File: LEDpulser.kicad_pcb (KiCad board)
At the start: 2 copper layers, 50.8 x 77.7 mm, 84 parts, among them J1 RJHSE-5380, J2 EPS.00.250.NTN, J3 EPS.00.250.NTN, J4 EB21A-04-D, J5 EPL.0S.302.HLN, Q1 DMP32D4S, Q2 DMN3028LQ-7, Q3 DMN3028LQ-7, SW1 BST11T2AVR, U1 74AHCT123APW,118, U10 LT3082EST#TRPBF, U2 74AHCT123APW,118, U3 74AHCT123APW,118, U4 SN74LVC2G74, U5 LT1117, U6 IXDI602SIATR, U7 NE555S-13, U8 PM8834, U9 PM8834

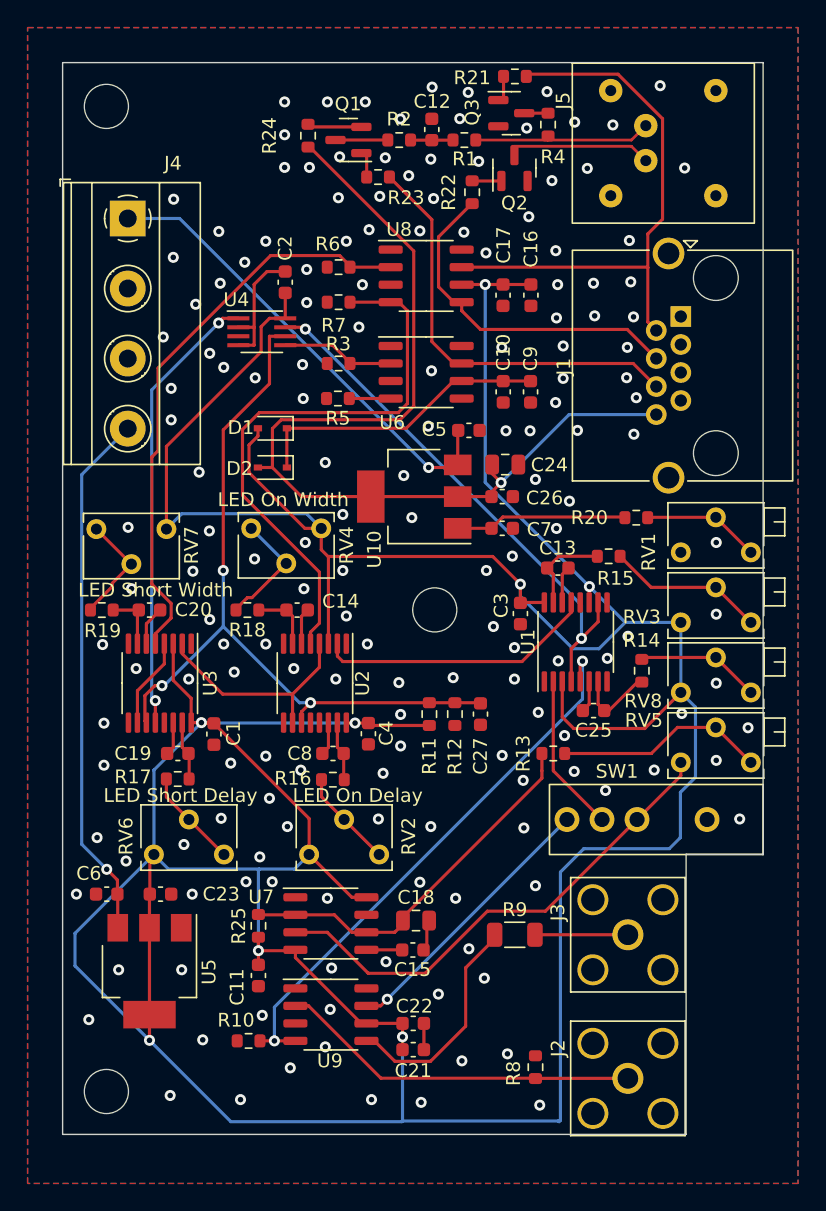
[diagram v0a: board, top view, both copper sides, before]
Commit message: Added guard ring around 0-20V regulator set pin and output to set current shunt.
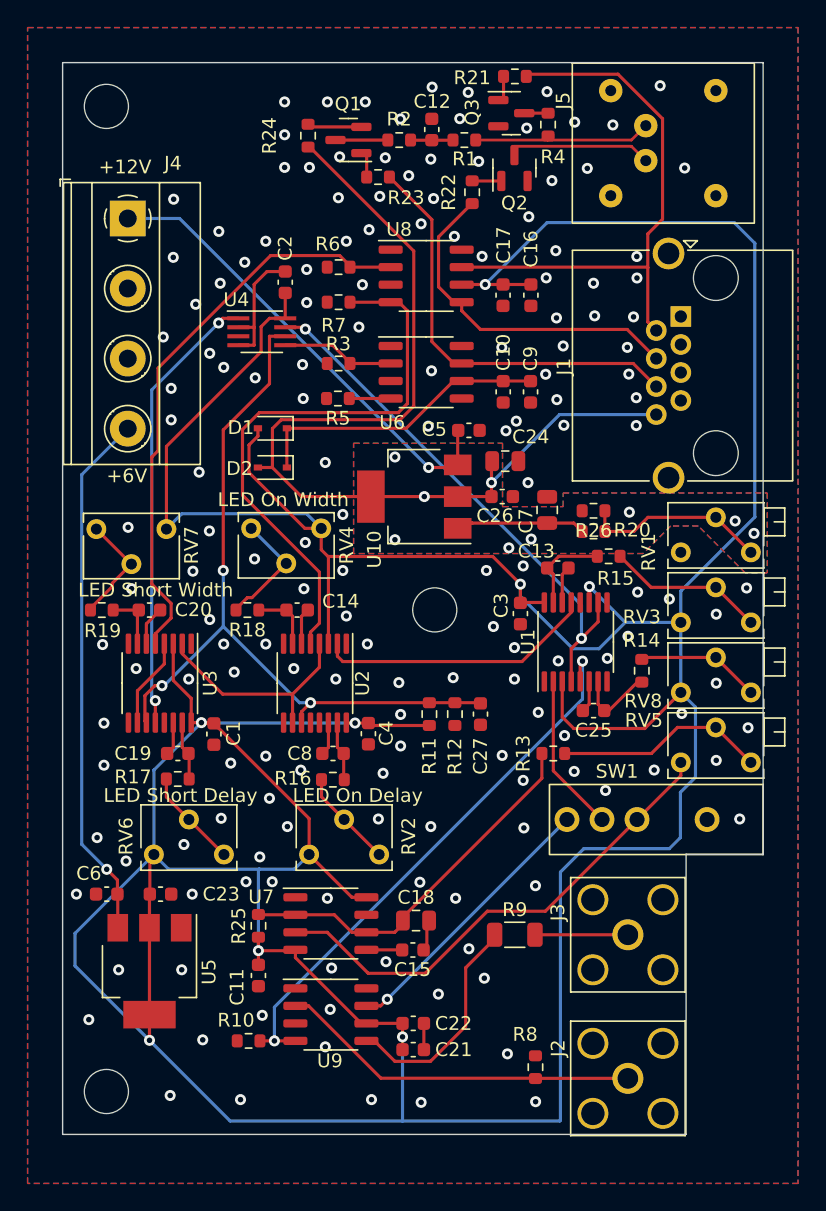
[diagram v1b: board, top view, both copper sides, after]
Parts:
- added R26: DNP, Resistor_SMD:R_0603_1608Metric, F.Cu at (127.4, 57.9)
- C7: value 1uF -> 0.1uF; footprint Capacitor_SMD:C_0603_1608Metric -> Capacitor_SMD:C_0805_2012Metric
- moved C7 3.52 mm to (124.0, 57.8), turned to 90 degrees
- moved R20 3.26 mm to (127.4, 59.4)
- moved C24 0.25 mm to (121.0, 54.3)
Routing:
- net VCC: track 335.3 -> 361.9 mm
- net Net-(R20-Pad1): track 8.55 -> 13.6 mm
- net Net-(C7-Pad1): track 12.5 -> 9.96 mm
- net /CAP_VOLTAGE_OUT: track 69.6 -> 70.1 mm, vias 1 -> 9
- net GND: vias 169 -> 165
- added copper zone on B.Cu, net /CAP_VOLTAGE_OUT
- added copper zone on F.Cu, net /CAP_VOLTAGE_OUT
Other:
- board text added: "+12V"

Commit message: Minor layout edits and generation of fabrication files.
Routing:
- net Net-(C7-Pad1): track 9.96 -> 9.43 mm
- net /CAP_VOLTAGE_OUT: track 70.1 -> 70.0 mm, vias 9 -> 10

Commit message: Added pdf schematic.
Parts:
- D1, D2: value CUS08F30,H3F -> CUS08F30
- U1, U2, U3: value 74AHCT123APW,118 -> 74AHCT123
- U10: value LT3082EST#TRPBF -> LT3082
- U6: value IXDI602SIATR -> IXDI602
- U7: value NE555S-13 -> NE555S

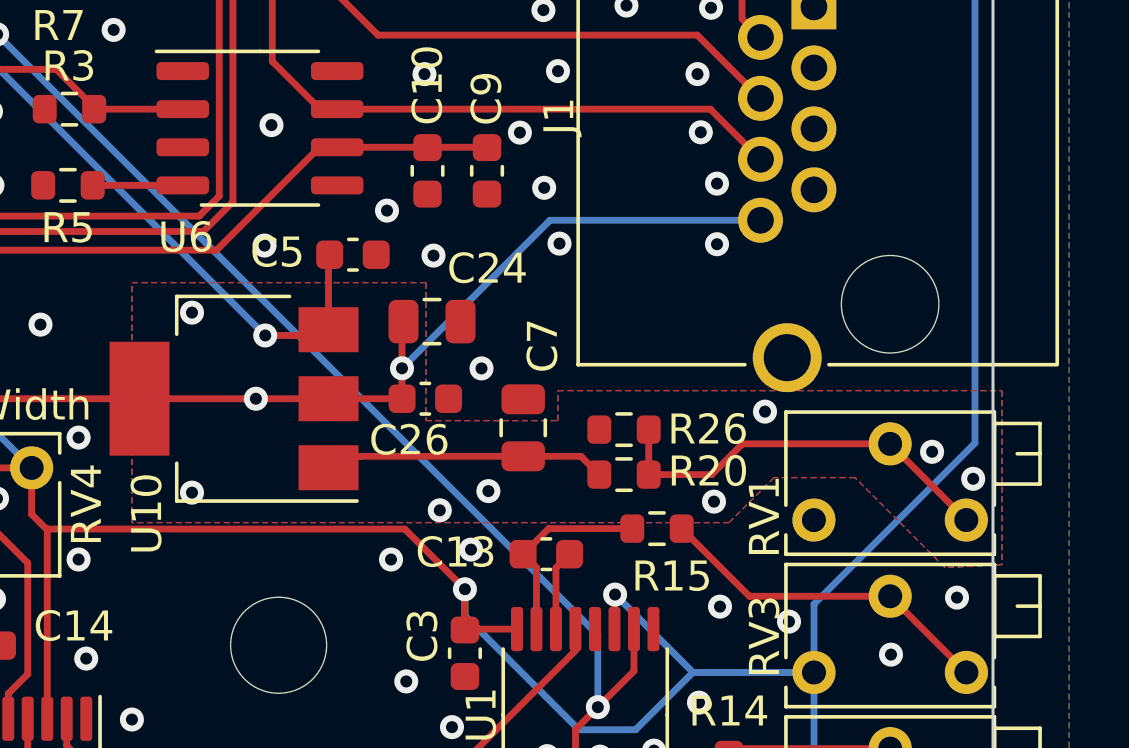
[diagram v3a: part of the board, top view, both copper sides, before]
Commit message: Fixed issue with shorts on RJ-45 connector shorting out HV regulator.
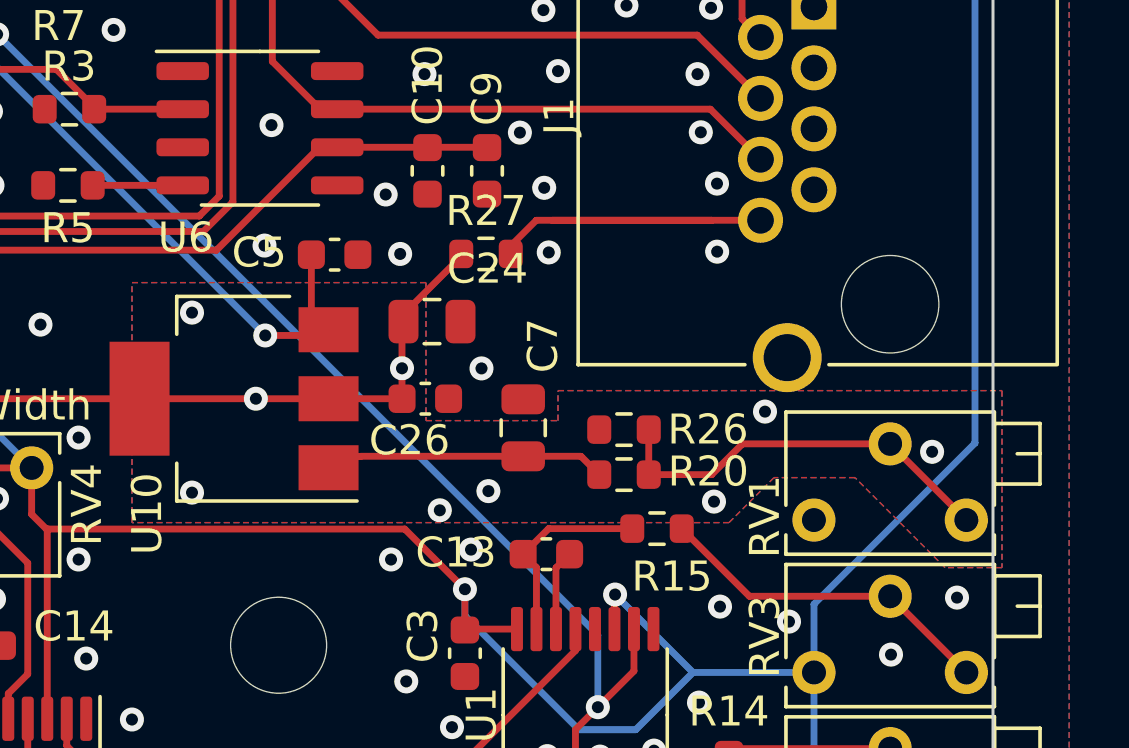
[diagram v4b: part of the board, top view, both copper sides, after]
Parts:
- added R27: 10k, Resistor_SMD:R_0603_1608Metric, F.Cu at (122.8, 52.0)
- D1, D2: value CUS08F30 -> CUS08F30,H3F
- R4: value 50 -> 0
- RV1: value 2Meg -> 100k
- U1, U2, U3: value 74AHCT123 -> 74AHCT123APW,118
- U10: value LT3082 -> LT3082EST#TRPBF
- U6: value IXDI602 -> IXDN602SIATR
- U7: value NE555S -> NE555S-13
- moved C5 0.61 mm to (117.8, 52.1)
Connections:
- C24 pad 1: /CAP_VOLTAGE_OUT -> /CAP_VOLTAGE
- C26 pad 1: /CAP_VOLTAGE_OUT -> /CAP_VOLTAGE
- D2 pad 2: /CAP_VOLTAGE_OUT -> /CAP_VOLTAGE
- R24 pad 2: /CAP_VOLTAGE_OUT -> /CAP_VOLTAGE
- R26 pad 2: /CAP_VOLTAGE_OUT -> /CAP_VOLTAGE
- U10 pad 2: /CAP_VOLTAGE_OUT -> /CAP_VOLTAGE
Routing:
- net /CAP_VOLTAGE: track 0.00 -> 60.1 mm, vias 0 -> 9
- net /CAP_VOLTAGE_OUT: track 70.0 -> 14.4 mm, vias 10 -> 0
- added copper zone on B.Cu, net /CAP_VOLTAGE
- added copper zone on F.Cu, net /CAP_VOLTAGE
- removed copper zone on B.Cu, net /CAP_VOLTAGE_OUT
- removed copper zone on F.Cu, net /CAP_VOLTAGE_OUT
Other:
- board text added: "LED Pulser v3"
- board text removed: "LED Pulser v2"

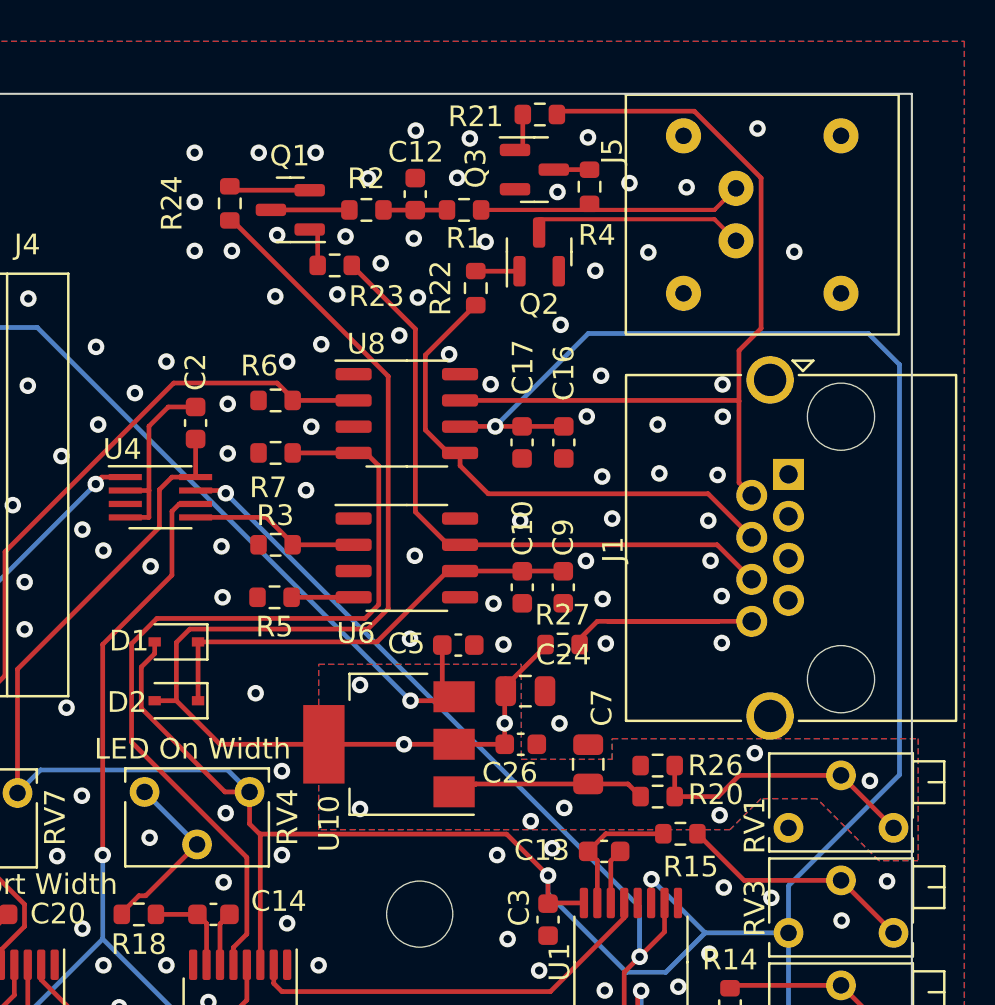
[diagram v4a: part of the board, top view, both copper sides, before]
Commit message: Added resistors to prevent shorting power through outputs on RJ45.
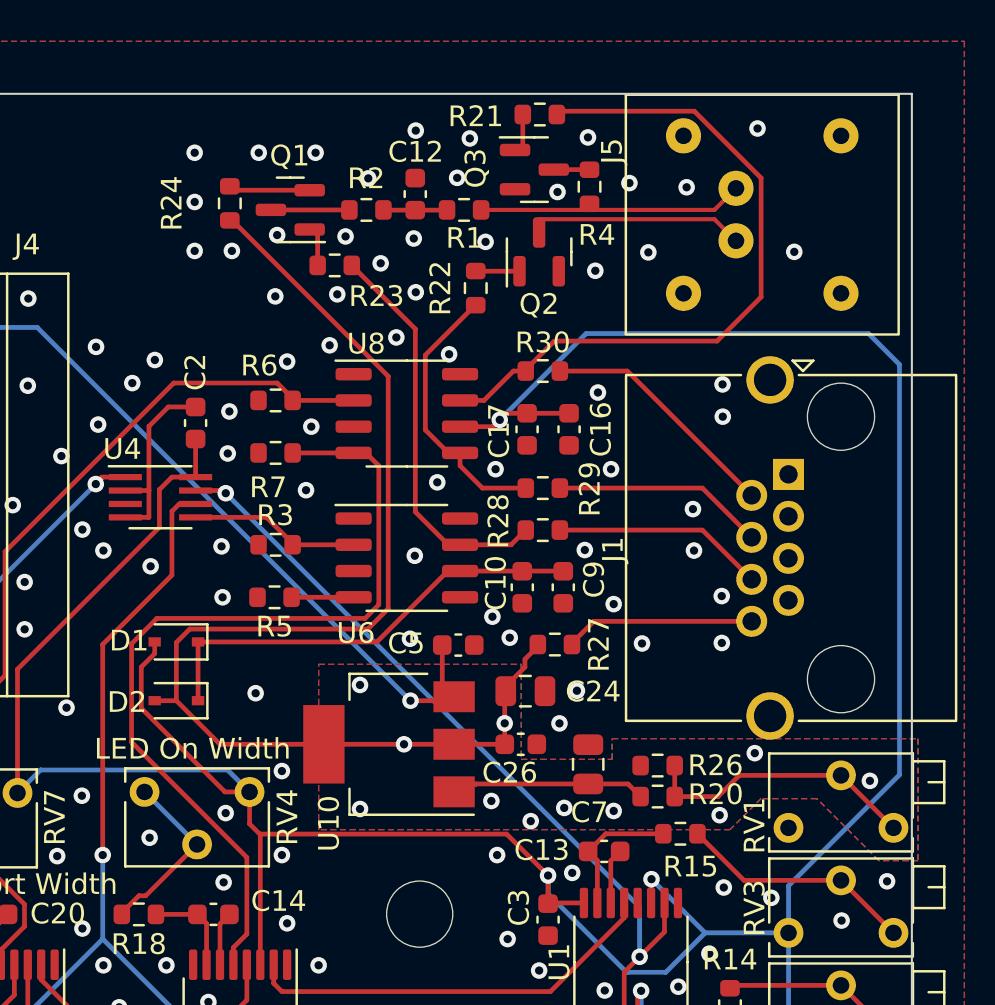
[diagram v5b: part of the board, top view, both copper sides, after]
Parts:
- added R28: 10k, Resistor_SMD:R_0603_1608Metric, F.Cu at (121.8, 46.5)
- added R29: 10k, Resistor_SMD:R_0603_1608Metric, F.Cu at (121.8, 44.5)
- added R30: 10k, Resistor_SMD:R_0603_1608Metric, F.Cu at (121.8, 38.8)
- added REF**: TUNL LOGO small, Library:TUNL LOGO small, B.Cu at (121.0, 38.1)
- moved C16 0.68 mm to (123.1, 41.6)
- moved C17 0.68 mm to (121.1, 41.6)
- moved R27 0.37 mm to (122.4, 52.0)
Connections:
- R21 pad 2: /LED_SHORT_OUT -> Net-(R21-Pad2)
- R22 pad 2: /LED_ON_OUT -> Net-(R22-Pad2)
- R23 pad 2: /CAP_CHARGING_OUT -> Net-(R23-Pad2)
- U6 pad 7: /CAP_CHARGING_OUT -> Net-(R23-Pad2)
- U8 pad 5: /LED_ON_OUT -> Net-(R22-Pad2)
- U8 pad 7: /LED_SHORT_OUT -> Net-(R21-Pad2)
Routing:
- net Net-(R21-Pad2): track 0.00 -> 33.7 mm
- net /LED_SHORT_OUT: track 40.8 -> 11.8 mm
- net /CAP_CHARGING_OUT: track 30.8 -> 10.3 mm
- net Net-(R23-Pad2): track 0.00 -> 19.5 mm
- net /LED_ON_OUT: track 24.8 -> 10.3 mm
- net Net-(R22-Pad2): track 0.00 -> 12.9 mm
- net /CAP_VOLTAGE_OUT: track 14.4 -> 9.20 mm
- net /CAP_VOLTAGE: track 60.1 -> 58.9 mm, vias 9 -> 11
- net GND: vias 165 -> 160
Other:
- board text added: "LED Pulser v4"
- board text removed: "LED Pulser v3"
